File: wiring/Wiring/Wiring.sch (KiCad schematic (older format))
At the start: 12 parts, among them U1 MAIN, U2 E, U3 F, U4 G

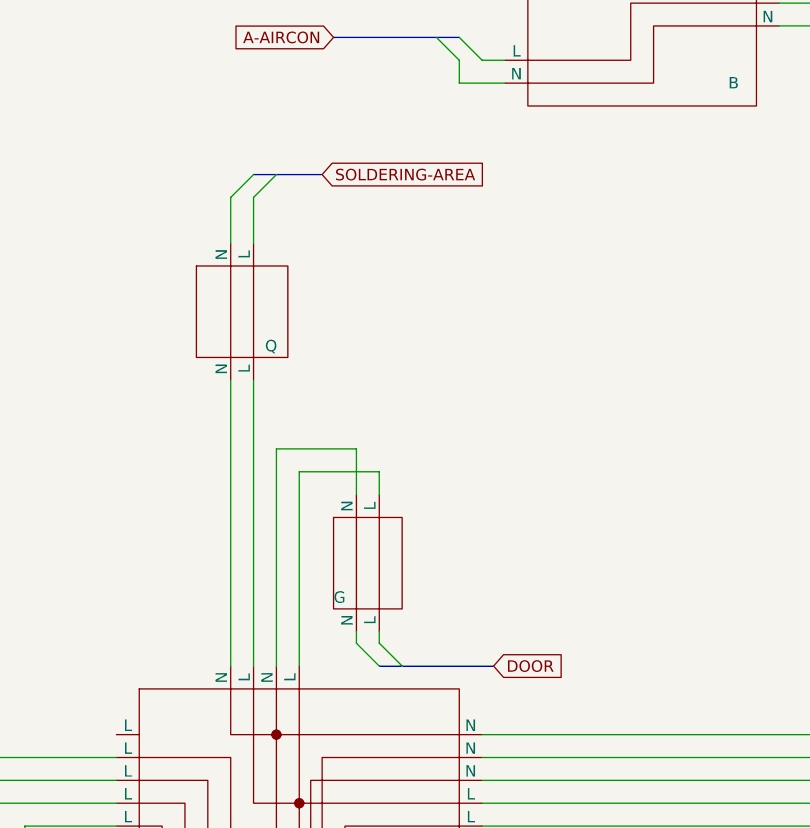
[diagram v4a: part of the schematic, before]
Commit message: Correctly wire input/output of Q
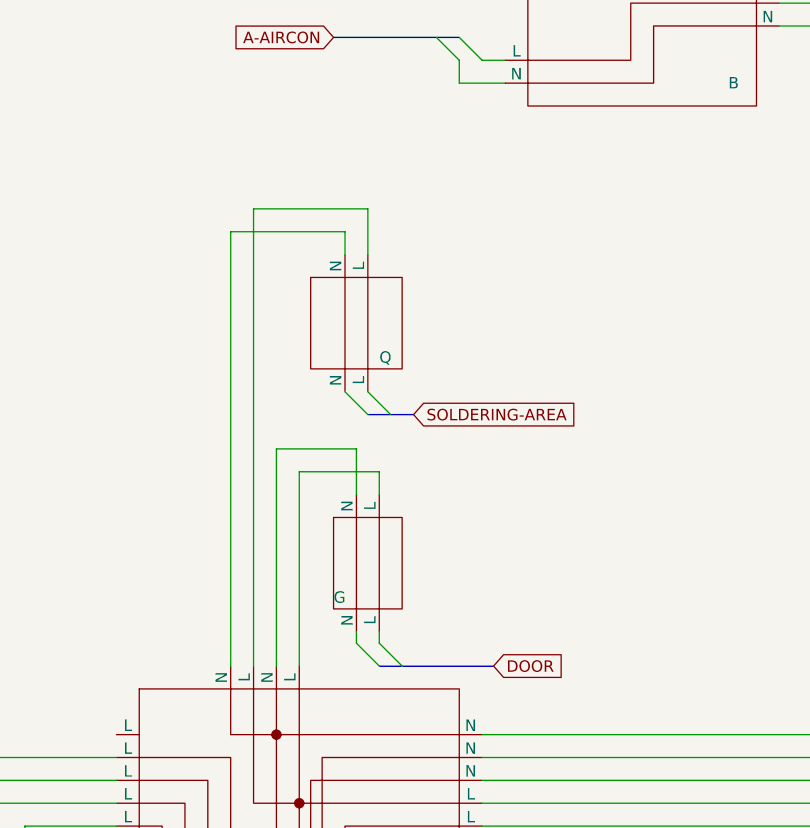
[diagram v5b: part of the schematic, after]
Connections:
- net at U3.~ (L): now also U?.10 (N); no longer U2.24 (L)
- net at U?.10 (N): no longer U3.~ (L)
- net at U2.~ (N): now also U?.12 (N); no longer U?.10 (N)
- net at U?.12 (N): no longer U2.~ (N)
- net at U1.~ (N): now also U?.16 (N)
- net at U?.12 (N): no longer U1.~ (N)
- net at U?.16 (N): no longer U1.~ (N)
- net at U?.~ (N): now also U?.12 (L)
- new net: U2.24 (L), U3.~ (L)
- new net: U2.14 (L), U?.12 (L)
- new net: U2.~ (N), U?.10 (N)
- new net: U1.~ (N), U?.12 (N)
- new net: U?.10 (N), U?.8 (N) (x2)
- new net: U?.12 (L), U?.9 (L) (x2)
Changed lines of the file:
@@
 Wire Wire Line
 	10700 7600 10700 11450
-Wire Wire Line
-	10500 4600 10500 3350
-Wire Wire Line
-	10400 4600 10400 3350
-Entry Wire Line
-	10400 2550 10500 2450
-Entry Wire Line
-	10500 2550 10600 2450
-Text GLabel 10800 2450 2    50   Input ~ 0
+Entry Wire Line
+	11000 3500 10900 3400
+Entry Wire Line
+	11100 3500 11000 3400
+Text GLabel 11200 3500 2    50   Input ~ 0
 SOLDERING-AREA
 Wire Wire Line
@@
 L Wiring:Q U?
 U 1 1 5EE2C972
-P 10450 3050
-F 0 "U?" H 10300 3200 50  0001 C CNN
-F 1 "Q" H 10550 2900 50  0000 L CNN
-F 2 "" H 9750 2900 50  0001 C CNN
-F 3 "" H 9750 2900 50  0001 C CNN
-	1    10450 3050
-	1    0    0    -1
-$EndComp
-Wire Wire Line
-	10500 2750 10500 2550
-Wire Wire Line
-	10400 2550 10400 2750
+P 10950 3100
+F 0 "U?" H 10800 3250 50  0001 C CNN
+F 1 "Q" H 11050 2950 50  0000 L CNN
+F 2 "" H 10250 2950 50  0001 C CNN
+F 3 "" H 10250 2950 50  0001 C CNN
+	1    10950 3100
+	1    0    0    -1
+$EndComp
 $Comp
 L Wiring:J U?
@@
 Wire Wire Line
 	17150 7100 14350 7100
+Wire Wire Line
+	10400 2700 10900 2700
+Wire Wire Line
+	10900 2700 10900 2800
+Wire Wire Line
+	10400 2700 10400 4600
+Wire Wire Line
+	10500 2600 11000 2600
+Wire Wire Line
+	11000 2600 11000 2800
+Wire Wire Line
+	10500 2600 10500 4600
 Wire Bus Line
 	15750 6100 15950 6100
@@
 	10850 1850 11400 1850
 Wire Bus Line
-	10500 2450 10800 2450
+	11000 3500 11200 3500
 Wire Bus Line
 	18250 7150 18600 7150
